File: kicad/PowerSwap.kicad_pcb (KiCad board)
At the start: 2 copper layers, 0 parts

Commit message: Started the layout
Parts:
- added C1: 4.7μF, Capacitors_SMD:C_0805_HandSoldering, F.Cu at (139.3, 94.8)
- added C2: 11μF, Capacitors_SMD:C_0805_HandSoldering, F.Cu at (149.7, 94.3)
- added C3: 0.1μF, Capacitors_SMD:C_0805_HandSoldering, F.Cu at (136.5, 97.3)
- added L1: 2.2μΗ, PowerSwap-Footprints:SRN3015, F.Cu at (145.8, 90.7)
- added R1: 0, Resistors_SMD:R_0805_HandSoldering, F.Cu at (141.7, 94.9)
- added R2: 0, Resistors_SMD:R_0805_HandSoldering, F.Cu at (146.1, 98.9)
- added R3: 0, Resistors_SMD:R_0805_HandSoldering, F.Cu at (140.6, 98.8)
- added R4: 2.1MΩ, Resistors_SMD:R_0805_HandSoldering, F.Cu at (154.7, 94.3)
- added R5: 215KΩ, Resistors_SMD:R_0805_HandSoldering, F.Cu at (152.0, 97.0)
- added TP+: Vin, Pin_Headers:Pin_Header_Straight_1x01, F.Cu at (133.0, 88.9)
- added TP+: Vout, Pin_Headers:Pin_Header_Straight_1x01, F.Cu at (158.5, 88.9)
- added TP-: GND, Pin_Headers:Pin_Header_Straight_1x01, F.Cu at (133.0, 99.5)
- added TP-: PGND, Pin_Headers:Pin_Header_Straight_1x01, F.Cu at (158.5, 99.6)
- added TP-FB1: Feedback, Pin_Headers:Pin_Header_Straight_1x01, F.Cu at (152.6, 102.1)
- added TP-L1: L1, Pin_Headers:Pin_Header_Straight_1x01, F.Cu at (141.2, 88.9)
- added TP-L2: L2, Pin_Headers:Pin_Header_Straight_1x01, F.Cu at (150.1, 88.9)
- added U1: TPS63030, PowerSwap-Footprints:TPS63030, F.Cu at (145.8, 94.7)
- added Vin: Battery, Pin_Headers:Pin_Header_Straight_1x02, F.Cu at (133.0, 93.0)
- added Vout: Vout, Pin_Headers:Pin_Header_Straight_1x02, F.Cu at (158.5, 93.0)
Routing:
- net Net-(C3-Pad1): track 0.00 -> 6.81 mm
- net Net-(R3-Pad1): track 0.00 -> 4.85 mm
- net Net-(L1-Pad1): track 0.00 -> 4.29 mm
- net Net-(L1-Pad2): track 0.00 -> 3.95 mm
- added copper zone on F.Cu, net /Vin+
- added copper zone on F.Cu, net /Vout+
- added copper zone on F.Cu, net GNDPWR
- added copper zone on F.Cu, net Net-(L1-Pad1)
- added copper zone on F.Cu, net Net-(L1-Pad2)
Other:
- net class Default: clearance 0.2 -> 0.254; trace_width 0.25 -> 0.254; via_dia 0.6 -> 0.6858; via_drill 0.4 -> 0.3302
- rule trace_clearance: 0.2 -> 0.254
- rule trace_min: 0.2 -> 0.1524
- rule via_min_drill: 0.3 -> 0.3302
- rule via_min_size: 0.4 -> 0.6858

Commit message: Completed layout
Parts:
- moved TP-L1 3.95 mm to (144.0, 86.1)
- moved R4 3.77 mm to (152.2, 91.5), turned to 90 degrees
- moved TP-L2 3.61 mm to (147.8, 86.1)
- moved R1 3.58 mm to (141.9, 91.3), turned to 270 degrees
- moved R3 1.42 mm to (140.6, 100.2)
- moved R2 1.32 mm to (146.1, 100.2)
- moved TP-FB1 0.57 mm to (152.0, 102.1)
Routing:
- net Net-(C3-Pad1): track 6.81 -> 36.3 mm, vias 0 -> 2
- net /Feedback: track 0.01 -> 21.4 mm, vias 0 -> 2
- net Net-(R2-Pad1): track 0.00 -> 4.89 mm
- net Net-(R3-Pad1): track 4.85 -> 6.47 mm, vias 0 -> 2
- net Net-(L1-Pad2): track 3.95 -> 5.03 mm
- net Net-(L1-Pad1): track 4.29 -> 5.05 mm
- added copper zone on B.Cu, net GNDPWR
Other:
- board outline added: 33.5 x 22.4 mm

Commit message: Final layout
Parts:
- removed C3: 0.1μF, Capacitors_SMD:C_0805_HandSoldering
- removed TP+: Vin, Pin_Headers:Pin_Header_Straight_1x01
- removed TP+: Vout, Pin_Headers:Pin_Header_Straight_1x01
- removed TP-: GND, Pin_Headers:Pin_Header_Straight_1x01
- removed TP-: PGND, Pin_Headers:Pin_Header_Straight_1x01
- removed TP-FB1: Feedback, Pin_Headers:Pin_Header_Straight_1x01
- removed TP-L1: L1, Pin_Headers:Pin_Header_Straight_1x01
- removed TP-L2: L2, Pin_Headers:Pin_Header_Straight_1x01
- removed Vin: Battery, Pin_Headers:Pin_Header_Straight_1x02
- removed Vout: Vout, Pin_Headers:Pin_Header_Straight_1x02
- added C4: 0.1μF, Capacitors_SMD:C_0805, F.Cu at (146.0, 98.3)
- added P1: Battery, Pin_Headers:Pin_Header_Straight_1x02, F.Cu at (136.8, 93.3)
- added P2: Vout, Pin_Headers:Pin_Header_Straight_1x02, F.Cu at (156.8, 93.0)
- added P3: TST, Pin_Headers:Pin_Header_Straight_1x01, F.Cu at (136.8, 99.6)
- added P4: TST, Pin_Headers:Pin_Header_Straight_1x01, F.Cu at (156.8, 99.3)
- added P5: TST, Pin_Headers:Pin_Header_Straight_1x01, F.Cu at (136.8, 89.7)
- added P6: TST, Measurement_Points:Measurement_Point_Square-SMD-Pad_Small, F.Cu at (143.0, 89.4)
- added P7: TST, Measurement_Points:Measurement_Point_Square-SMD-Pad_Small, F.Cu at (148.7, 89.3)
- added P8: TST, Pin_Headers:Pin_Header_Straight_1x01, F.Cu at (156.7, 89.3)
- added P9: TST, Measurement_Points:Measurement_Point_Square-SMD-Pad_Small, F.Cu at (153.6, 96.3)
- C1: footprint Capacitors_SMD:C_0805_HandSoldering -> Capacitors_SMD:C_0805
- C2: value 11μF -> 22μF; footprint Capacitors_SMD:C_0805_HandSoldering -> Capacitors_SMD:C_1210
- R1: value 0 -> 2.1MΩ; footprint Resistors_SMD:R_0805_HandSoldering -> Resistors_SMD:R_0805
- R2: value 0 -> 215KΩ; footprint Resistors_SMD:R_0805_HandSoldering -> Resistors_SMD:R_0805
- R3: footprint Resistors_SMD:R_0805_HandSoldering -> Resistors_SMD:R_0805
- R4: value 2.1MΩ -> 0; footprint Resistors_SMD:R_0805_HandSoldering -> Resistors_SMD:R_0805
- R5: value 215KΩ -> 0; footprint Resistors_SMD:R_0805_HandSoldering -> Resistors_SMD:R_0805
- moved R4 12.1 mm to (144.8, 101.1)
- moved R1 11.4 mm to (151.3, 97.7), turned to 90 degrees
- moved R5 6.22 mm to (147.3, 101.1)
- moved R2 3.82 mm to (148.9, 97.7), turned to 270 degrees
- moved C1 3.31 mm to (142.6, 94.6)
- moved R3 2.22 mm to (142.6, 101.1), turned to 270 degrees
- moved C2 0.74 mm to (149.4, 93.6)
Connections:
- net Net-(L1-Pad1) renamed /L1
- net Net-(L1-Pad2) renamed /L2
- R1 pad 1: Net-(C3-Pad1) -> /Vout+
- R1 pad 2: /Vin+ -> /Feedback
- R2 pad 1: Net-(R2-Pad1) -> /Feedback
- R2 pad 2: Net-(C3-Pad1) -> GNDPWR
- R3 pad 1: Net-(R3-Pad1) -> /Vina
- R3 pad 2: Net-(C3-Pad1) -> /Vin+
- R4 pad 1: /Vout+ -> /EN
- R4 pad 2: /Feedback -> /Vina
- R5 pad 1: /Feedback -> /PS
- R5 pad 2: GNDPWR -> /Vina
- U1 pad 6: Net-(R2-Pad1) -> /EN
- U1 pad 7: Net-(R3-Pad1) -> /PS
- U1 pad 8: Net-(C3-Pad1) -> /Vina
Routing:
- net Net-(C3-Pad1): track 36.3 -> 0.00 mm, vias 2 -> 0
- net /Feedback: track 21.4 -> 7.26 mm, vias 2 -> 0
- net /PS: track 0.00 -> 14.0 mm
- net /EN: track 0.00 -> 11.5 mm
- net /Vin+: track 0.00 -> 11.3 mm, vias 0 -> 2
- net /Vina: track 0.00 -> 9.24 mm
- net /Vout+: track 0.00 -> 7.45 mm, vias 0 -> 2
- net Net-(R3-Pad1): track 6.47 -> 0.00 mm, vias 2 -> 0
- net Net-(R2-Pad1): track 4.89 -> 0.00 mm
- net /L2: track 5.03 -> 5.97 mm
- net /L1: track 5.05 -> 5.69 mm
- removed copper zone on F.Cu, net /L1
- removed copper zone on F.Cu, net /L2
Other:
- board size 33.5 x 22.4 mm -> 23.9 x 17.8 mm

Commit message: Completed the layout and gerbers
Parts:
- added REF**11: VIA-0.6mm, PowerSwap-Footprints:VIA-0.6mm, F.Cu at (141.1, 96.9)
- added REF**111: VIA-0.6mm, PowerSwap-Footprints:VIA-0.6mm, F.Cu at (149.1, 100.1)
- added REF**1111: VIA-0.6mm, PowerSwap-Footprints:VIA-0.6mm, F.Cu at (135.7, 102.0)
- added REF**1112: VIA-0.6mm, PowerSwap-Footprints:VIA-0.6mm, F.Cu at (135.7, 103.0)
- added REF**1113: VIA-0.6mm, PowerSwap-Footprints:VIA-0.6mm, F.Cu at (135.7, 104.0)
- added REF**112: VIA-0.6mm, PowerSwap-Footprints:VIA-0.6mm, F.Cu at (149.1, 101.1)
- added REF**1121: VIA-0.6mm, PowerSwap-Footprints:VIA-0.6mm, F.Cu at (136.7, 102.0)
- added REF**1122: VIA-0.6mm, PowerSwap-Footprints:VIA-0.6mm, F.Cu at (136.7, 103.0)
- added REF**1123: VIA-0.6mm, PowerSwap-Footprints:VIA-0.6mm, F.Cu at (136.7, 104.0)
- added REF**113: VIA-0.6mm, PowerSwap-Footprints:VIA-0.6mm, F.Cu at (149.1, 102.1)
- added REF**11311: VIA-0.6mm, PowerSwap-Footprints:VIA-0.6mm, F.Cu at (137.7, 102.0)
- added REF**1131101: VIA-0.6mm, PowerSwap-Footprints:VIA-0.6mm, F.Cu at (146.7, 103.0)
- added REF**1131102: VIA-0.6mm, PowerSwap-Footprints:VIA-0.6mm, F.Cu at (146.7, 104.0)
- added REF**113111: VIA-0.6mm, PowerSwap-Footprints:VIA-0.6mm, F.Cu at (137.7, 103.0)
- added REF**1131111: VIA-0.6mm, PowerSwap-Footprints:VIA-0.6mm, F.Cu at (147.7, 103.0)
- added REF**1131112: VIA-0.6mm, PowerSwap-Footprints:VIA-0.6mm, F.Cu at (147.7, 104.0)
- added REF**113112: VIA-0.6mm, PowerSwap-Footprints:VIA-0.6mm, F.Cu at (137.7, 104.0)
- added REF**113121: VIA-0.6mm, PowerSwap-Footprints:VIA-0.6mm, F.Cu at (138.7, 103.0)
- added REF**113122: VIA-0.6mm, PowerSwap-Footprints:VIA-0.6mm, F.Cu at (138.7, 104.0)
- added REF**113131: VIA-0.6mm, PowerSwap-Footprints:VIA-0.6mm, F.Cu at (139.7, 103.0)
- added REF**113132: VIA-0.6mm, PowerSwap-Footprints:VIA-0.6mm, F.Cu at (139.7, 104.0)
- added REF**113141: VIA-0.6mm, PowerSwap-Footprints:VIA-0.6mm, F.Cu at (140.7, 103.0)
- added REF**113142: VIA-0.6mm, PowerSwap-Footprints:VIA-0.6mm, F.Cu at (140.7, 104.0)
- added REF**113151: VIA-0.6mm, PowerSwap-Footprints:VIA-0.6mm, F.Cu at (141.7, 103.0)
- added REF**113152: VIA-0.6mm, PowerSwap-Footprints:VIA-0.6mm, F.Cu at (141.7, 104.0)
- added REF**113161: VIA-0.6mm, PowerSwap-Footprints:VIA-0.6mm, F.Cu at (142.7, 103.0)
- added REF**113162: VIA-0.6mm, PowerSwap-Footprints:VIA-0.6mm, F.Cu at (142.7, 104.0)
- added REF**113171: VIA-0.6mm, PowerSwap-Footprints:VIA-0.6mm, F.Cu at (143.7, 103.0)
- added REF**113172: VIA-0.6mm, PowerSwap-Footprints:VIA-0.6mm, F.Cu at (143.7, 104.0)
- added REF**113181: VIA-0.6mm, PowerSwap-Footprints:VIA-0.6mm, F.Cu at (144.7, 103.0)
- added REF**113182: VIA-0.6mm, PowerSwap-Footprints:VIA-0.6mm, F.Cu at (144.7, 104.0)
- added REF**113191: VIA-0.6mm, PowerSwap-Footprints:VIA-0.6mm, F.Cu at (145.7, 103.0)
- added REF**113192: VIA-0.6mm, PowerSwap-Footprints:VIA-0.6mm, F.Cu at (145.7, 104.0)
- added REF**11321: VIA-0.6mm, PowerSwap-Footprints:VIA-0.6mm, F.Cu at (138.7, 102.0)
- added REF**114: VIA-0.6mm, PowerSwap-Footprints:VIA-0.6mm, F.Cu at (149.1, 103.1)
- added REF**115: VIA-0.6mm, PowerSwap-Footprints:VIA-0.6mm, F.Cu at (149.1, 104.1)
- added REF**12: VIA-0.6mm, PowerSwap-Footprints:VIA-0.6mm, F.Cu at (141.1, 97.9)
- added REF**121: VIA-0.6mm, PowerSwap-Footprints:VIA-0.6mm, F.Cu at (150.1, 100.1)
- added REF**122: VIA-0.6mm, PowerSwap-Footprints:VIA-0.6mm, F.Cu at (150.1, 101.1)
- added REF**123: VIA-0.6mm, PowerSwap-Footprints:VIA-0.6mm, F.Cu at (150.1, 102.1)
- added REF**124: VIA-0.6mm, PowerSwap-Footprints:VIA-0.6mm, F.Cu at (150.1, 103.1)
- added REF**125: VIA-0.6mm, PowerSwap-Footprints:VIA-0.6mm, F.Cu at (150.1, 104.1)
- added REF**131: VIA-0.6mm, PowerSwap-Footprints:VIA-0.6mm, F.Cu at (151.1, 100.1)
- added REF**132: VIA-0.6mm, PowerSwap-Footprints:VIA-0.6mm, F.Cu at (151.1, 101.1)
- added REF**133: VIA-0.6mm, PowerSwap-Footprints:VIA-0.6mm, F.Cu at (151.1, 102.1)
- added REF**134: VIA-0.6mm, PowerSwap-Footprints:VIA-0.6mm, F.Cu at (151.1, 103.1)
- added REF**135: VIA-0.6mm, PowerSwap-Footprints:VIA-0.6mm, F.Cu at (151.1, 104.1)
- added REF**141: VIA-0.6mm, PowerSwap-Footprints:VIA-0.6mm, F.Cu at (152.1, 100.1)
- added REF**142: VIA-0.6mm, PowerSwap-Footprints:VIA-0.6mm, F.Cu at (152.1, 101.1)
- added REF**143: VIA-0.6mm, PowerSwap-Footprints:VIA-0.6mm, F.Cu at (152.1, 102.1)
- added REF**144: VIA-0.6mm, PowerSwap-Footprints:VIA-0.6mm, F.Cu at (152.1, 103.1)
- added REF**145: VIA-0.6mm, PowerSwap-Footprints:VIA-0.6mm, F.Cu at (152.1, 104.1)
- added REF**151: VIA-0.6mm, PowerSwap-Footprints:VIA-0.6mm, F.Cu at (153.1, 100.1)
- added REF**152: VIA-0.6mm, PowerSwap-Footprints:VIA-0.6mm, F.Cu at (153.1, 101.1)
- added REF**153: VIA-0.6mm, PowerSwap-Footprints:VIA-0.6mm, F.Cu at (153.1, 102.1)
- added REF**154: VIA-0.6mm, PowerSwap-Footprints:VIA-0.6mm, F.Cu at (153.1, 103.1)
- added REF**155: VIA-0.6mm, PowerSwap-Footprints:VIA-0.6mm, F.Cu at (153.1, 104.1)
- added REF**161: VIA-0.6mm, PowerSwap-Footprints:VIA-0.6mm, F.Cu at (154.1, 100.1)
- added REF**162: VIA-0.6mm, PowerSwap-Footprints:VIA-0.6mm, F.Cu at (154.1, 101.1)
- added REF**163: VIA-0.6mm, PowerSwap-Footprints:VIA-0.6mm, F.Cu at (154.1, 102.1)
- added REF**164: VIA-0.6mm, PowerSwap-Footprints:VIA-0.6mm, F.Cu at (154.1, 103.1)
- added REF**165: VIA-0.6mm, PowerSwap-Footprints:VIA-0.6mm, F.Cu at (154.1, 104.1)
- added REF**171: VIA-0.6mm, PowerSwap-Footprints:VIA-0.6mm, F.Cu at (155.1, 100.1)
- added REF**172: VIA-0.6mm, PowerSwap-Footprints:VIA-0.6mm, F.Cu at (155.1, 101.1)
- added REF**173: VIA-0.6mm, PowerSwap-Footprints:VIA-0.6mm, F.Cu at (155.1, 102.1)
- added REF**174: VIA-0.6mm, PowerSwap-Footprints:VIA-0.6mm, F.Cu at (155.1, 103.1)
- added REF**175: VIA-0.6mm, PowerSwap-Footprints:VIA-0.6mm, F.Cu at (155.1, 104.1)
- added REF**182: VIA-0.6mm, PowerSwap-Footprints:VIA-0.6mm, F.Cu at (156.1, 101.1)
- added REF**183: VIA-0.6mm, PowerSwap-Footprints:VIA-0.6mm, F.Cu at (156.1, 102.1)
- added REF**184: VIA-0.6mm, PowerSwap-Footprints:VIA-0.6mm, F.Cu at (156.1, 103.1)
- added REF**185: VIA-0.6mm, PowerSwap-Footprints:VIA-0.6mm, F.Cu at (156.1, 104.1)
- added REF**192: VIA-0.6mm, PowerSwap-Footprints:VIA-0.6mm, F.Cu at (157.1, 101.1)
- added REF**193: VIA-0.6mm, PowerSwap-Footprints:VIA-0.6mm, F.Cu at (157.1, 102.1)
- added REF**194: VIA-0.6mm, PowerSwap-Footprints:VIA-0.6mm, F.Cu at (157.1, 103.1)
- added REF**195: VIA-0.6mm, PowerSwap-Footprints:VIA-0.6mm, F.Cu at (157.1, 104.1)
- added REF**21: VIA-0.6mm, PowerSwap-Footprints:VIA-0.6mm, F.Cu at (142.1, 96.9)
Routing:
- net /Vin+: track 11.3 -> 17.3 mm, vias 2 -> 1
- net /Vout+: track 7.45 -> 10.7 mm, vias 2 -> 1
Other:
- board size 23.9 x 17.8 mm -> 23.9 x 18.6 mm
- board text added: "PowerSwap Rev 2L.1"

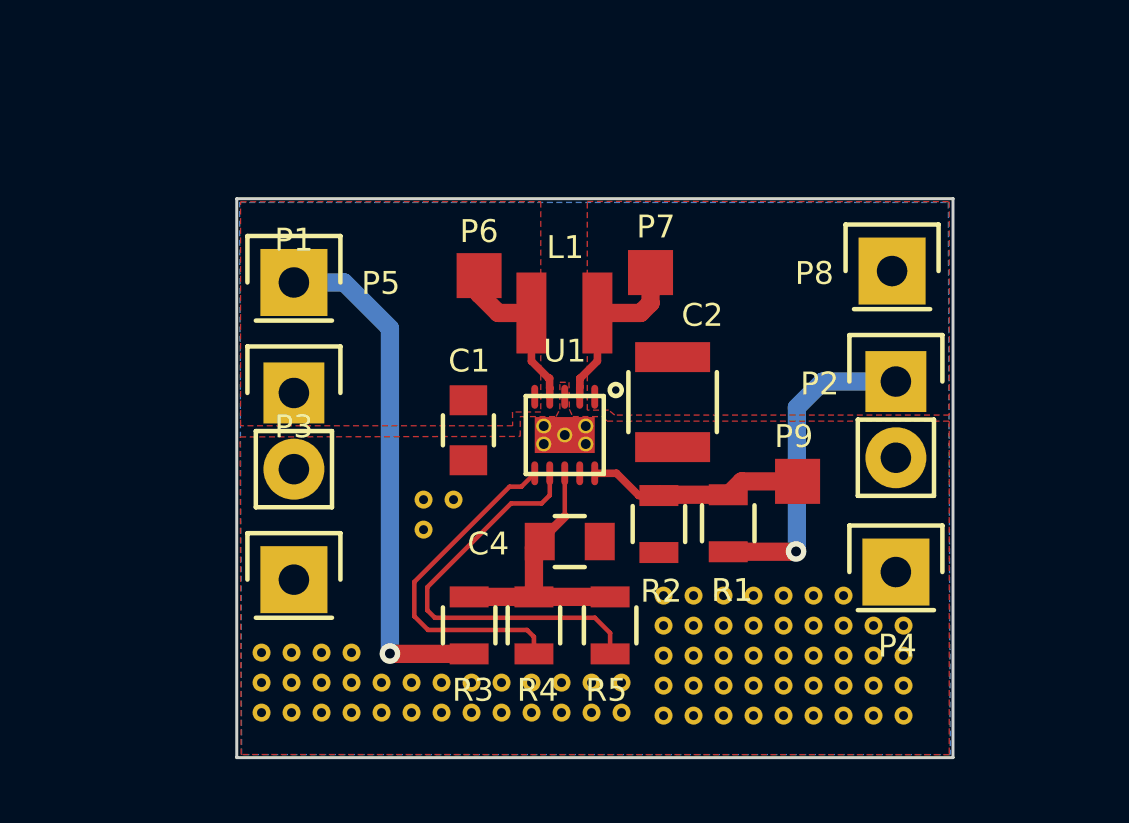
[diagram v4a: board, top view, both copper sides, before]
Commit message: Fixed the TPS63030 footprint and cleaned up the layout
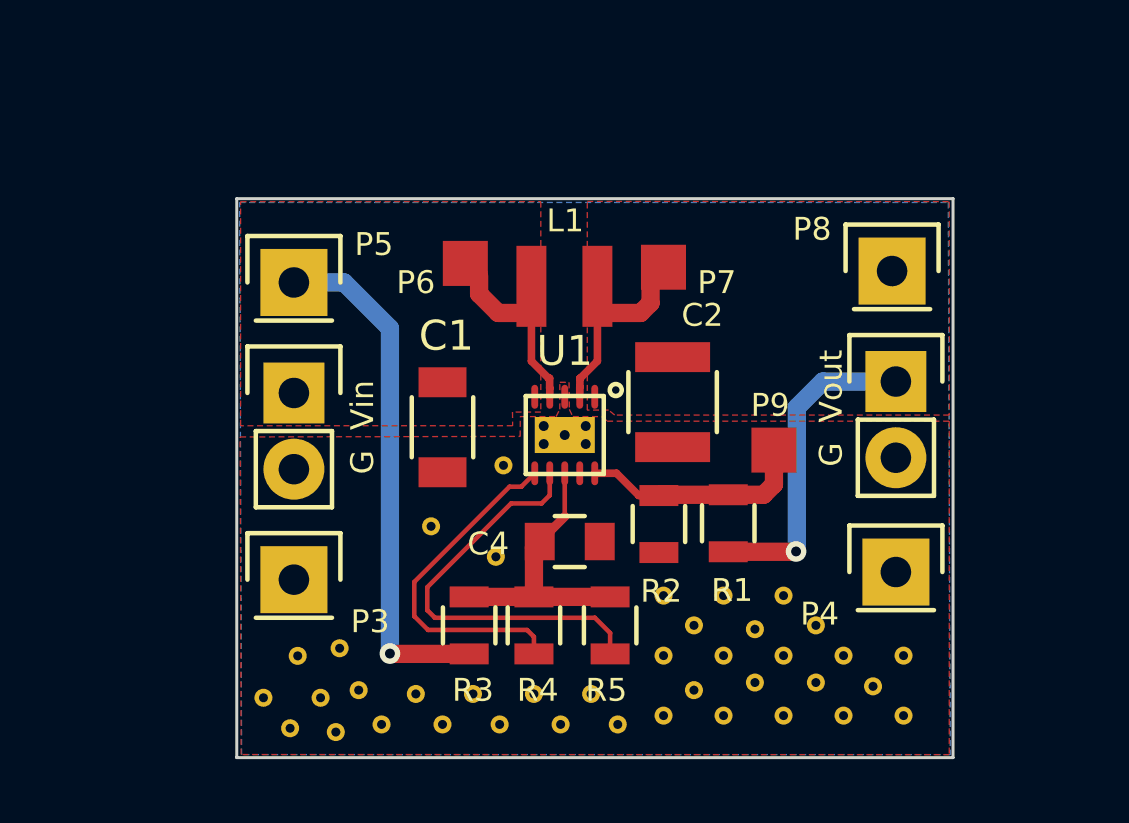
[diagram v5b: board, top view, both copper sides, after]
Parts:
- removed REF**1112, REF**112, REF**1122, REF**1131101, REF**113111, REF**1131111, REF**113121, REF**113122, REF**113131, REF**113141, REF**113151, REF**113161, REF**113171, REF**113181, REF**113191, REF**114, REF**121, REF**122, REF**124, REF**132, REF**134, REF**142, REF**144, REF**145, REF**152, REF**154, REF**162, REF**164, REF**165, REF**171, REF**172, REF**174, REF**182, REF**184, REF**185, REF**192, REF**194: VIA-0.6mm, PowerSwap-Footprints:VIA-0.6mm
- C1: footprint Capacitors_SMD:C_0805 -> Capacitors_SMD:C_1206
- R1: value 2.1MΩ -> 1.2MΩ
- moved REF**1121 3.03 mm to (138.2, 104.6)
- moved REF**11 2.90 mm to (143.8, 95.8)
- moved REF**21 2.37 mm to (143.5, 98.8)
- moved P9 1.31 mm to (152.8, 95.2)
- moved REF**11321 1.27 mm to (138.9, 103.3)
- moved REF**1111 1.21 mm to (136.9, 102.1)
- moved REF**141 1.12 mm to (152.1, 101.2)
- moved REF**183 1.02 mm to (156.1, 103.1)
- moved REF**123 1.01 mm to (150.1, 101.1)
- moved REF**161 1.00 mm to (154.2, 101.1)
- moved REF**163 0.90 mm to (154.2, 103.0)
- moved REF**143 0.90 mm to (152.1, 103.0)
- moved L1 0.89 mm to (145.8, 89.8)
- moved C1 0.87 mm to (141.7, 94.5)
- moved REF**125 0.85 mm to (150.1, 103.3)
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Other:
- net class Default: clearance 0.254 -> 0.1524; trace_width 0.254 -> 0.1524
- rule trace_clearance: 0.254 -> 0.1524
- board text added: "G Vin"
- board text added: "G Vout"

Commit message: Created Gerbers for 2L.2-c220856
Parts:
- moved REF**1111 0.41 mm to (136.7, 101.8)
- moved REF**113112 0.36 mm to (137.4, 103.3)
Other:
- board text added: "PowerSwap Rev 2L.2-c220856"
- board text removed: "PowerSwap Rev 2L.1"
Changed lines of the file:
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@@
     (links 75)
     (no_connects 0)
-    (area 134.823999 86.817999 158.800001 105.550001)
+    (area 131.297506 85.3428 161.565495 106.8454)
     (thickness 1.6)
     (drawings 7)
@@
     (pcbplotparams
       (layerselection 0x010fc_80000001)
-      (usegerberextensions true)
+      (usegerberextensions false)
       (excludeedgelayer true)
       (linewidth 0.127000)
@@
   )
   (module PowerSwap-Footprints:VIA-0.6mm (layer F.Cu)
-    (at 137.668 103.505)
+    (at 137.414 103.251)
     (fp_text reference REF**113112 (at 0 1.27) (layer F.SilkS) hide
       (effects (font (size 1 1) (thickness 0.15)))
@@
   )
   (module PowerSwap-Footprints:VIA-0.6mm (layer F.Cu)
-    (at 136.906 102.108)
+    (at 136.652 101.7905)
     (fp_text reference REF**1111 (at 0 1.27) (layer F.SilkS) hide
       (effects (font (size 1 1) (thickness 0.15)))
@@
     (effects (font (size 0.762 0.762) (thickness 0.127)))
   )
-  (gr_text "PowerSwap \nRev 2L.1\n" (at 148.9 90) (layer B.SilkS)
-    (effects (font (size 1.27 1.27) (thickness 0.254)) (justify mirror))
+  (gr_text "PowerSwap \nRev 2L.2-c220856\n" (at 154.178 89.281) (layer B.SilkS)
+    (effects (font (size 0.762 0.762) (thickness 0.127)) (justify left mirror))
   )
   (gr_line (start 134.874 105.5) (end 134.874 86.868) (angle 90) (layer Edge.Cuts) (width 0.1))
